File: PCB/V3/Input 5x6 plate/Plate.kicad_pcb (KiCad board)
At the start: 2 copper layers, 119.4 x 100.3 mm, 36 parts

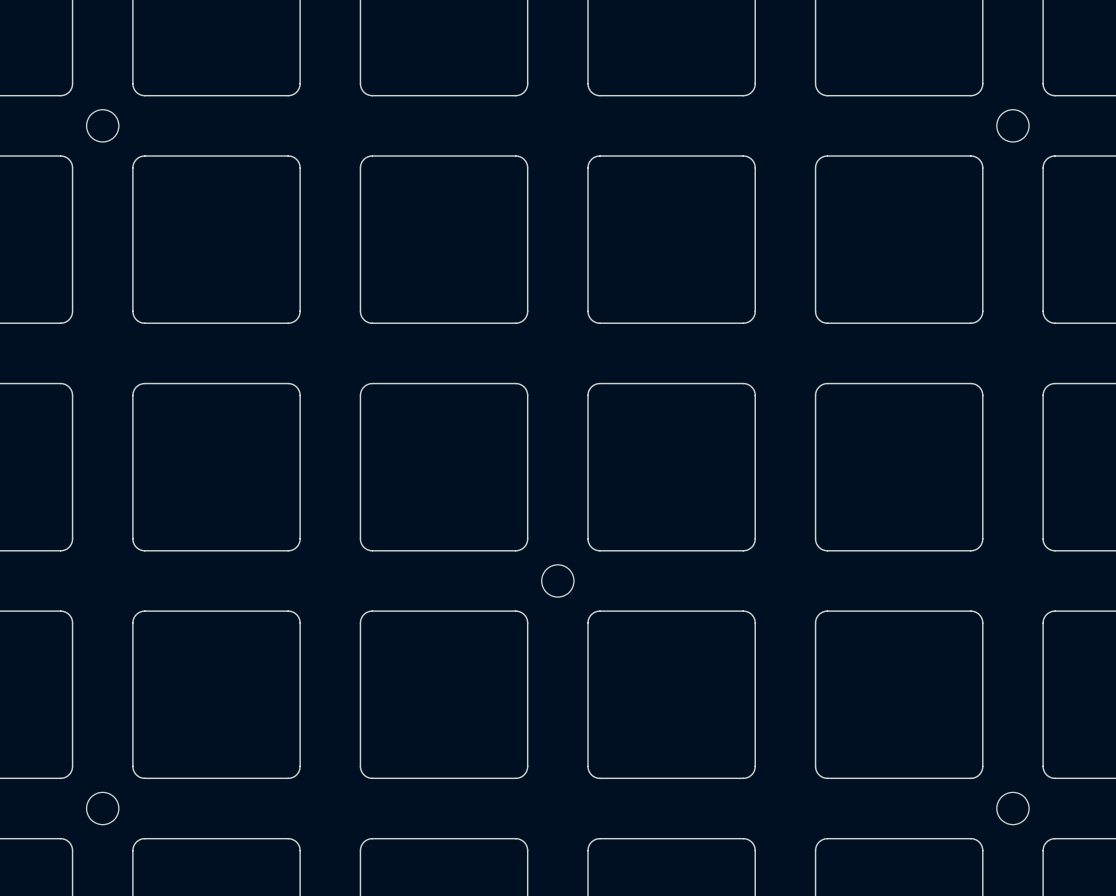
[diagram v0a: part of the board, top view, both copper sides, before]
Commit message: fix mount hole dimension
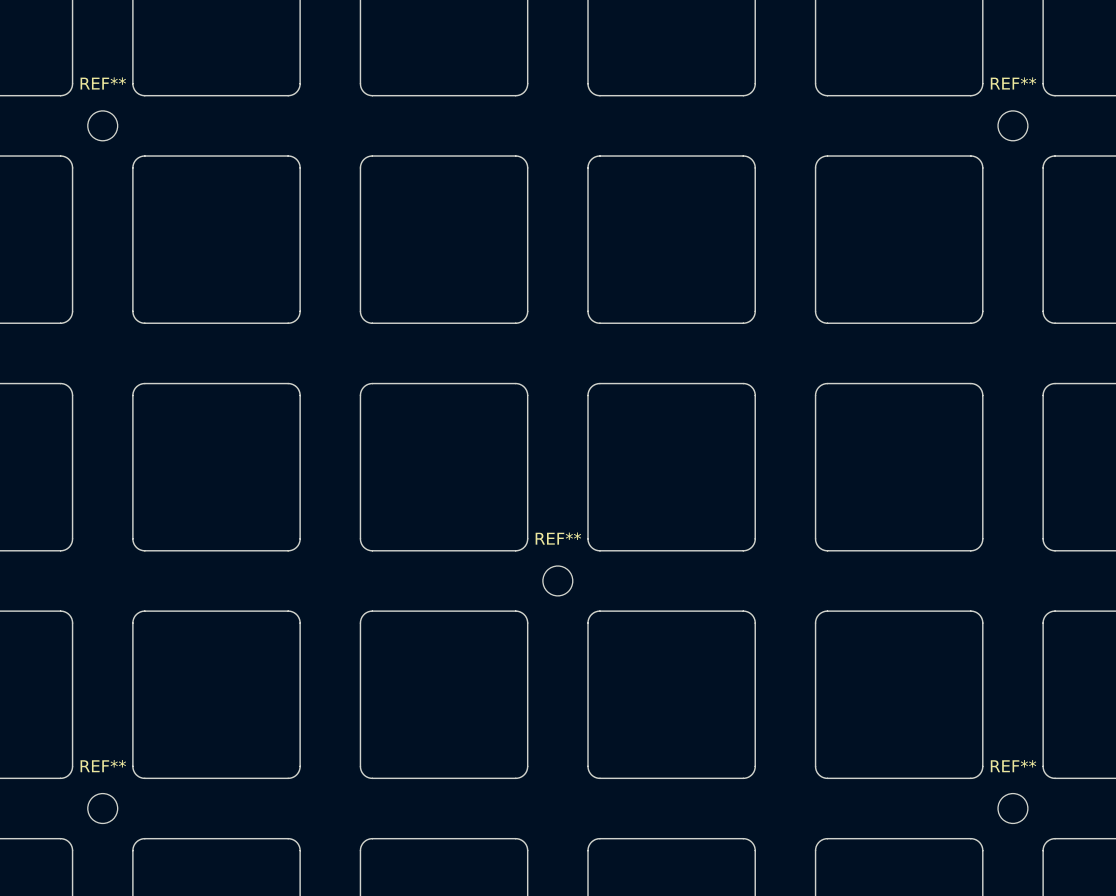
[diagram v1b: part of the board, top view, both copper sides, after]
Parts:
- REF** (x5): value MountingHole_2.7mm_M2.5 -> MountingHole_2.5mm; footprint MountingHole:MountingHole_2.7mm_M2.5 -> Keyboard_JSA:MountingHole_2.5mm
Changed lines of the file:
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@@
     (fp_arc (start 7 6) (mid 6.707107 6.707107) (end 6 7) (layer "Edge.Cuts") (width 0.12))
   )
-  (footprint "MountingHole:MountingHole_2.7mm_M2.5" (layer "F.Cu")
+  (footprint "Keyboard_JSA:MountingHole_2.5mm" (layer "F.Cu")
     (at 117.475 98.425)
-    (descr "Mounting Hole 2.7mm, no annular, M2.5")
-    (tags "mounting hole 2.7mm no annular m2.5")
+    (descr "Mounting Hole 2.5mm, no annular")
+    (tags "mounting hole 2.5mm no annular")
     (attr exclude_from_pos_files exclude_from_bom)
-    (fp_text reference "REF**" (at 0 -3.7) (layer "Dwgs.User")
-      (effects (font (size 1 1) (thickness 0.15)))
-    )
-    (fp_text value "MountingHole_2.7mm_M2.5" (at 0 3.7) (layer "F.Fab")
-      (effects (font (size 1 1) (thickness 0.15)))
-    )
-    (fp_text user "${REFERENCE}" (at 0.3 0) (layer "F.Fab")
-      (effects (font (size 1 1) (thickness 0.15)))
-    )
-    (fp_circle (center 0 0) (end 2.7 0) (layer "Cmts.User") (width 0.15) (fill none))
-    (fp_circle (center 0 0) (end 2.95 0) (layer "F.CrtYd") (width 0.05) (fill none))
-    (pad "" np_thru_hole circle (at 0 0) (size 2.7 2.7) (drill 2.7) (layers *.Cu *.Mask))
+    (fp_text reference "REF**" (at 0 -3.5) (layer "F.SilkS")
+      (effects (font (size 1 1) (thickness 0.15)))
+    )
+    (fp_text value "MountingHole_2.5mm" (at 0 3.5) (layer "F.Fab")
+      (effects (font (size 1 1) (thickness 0.15)))
+    )
+    (fp_text user "${REFERENCE}" (at 0 0) (layer "F.Fab")
+      (effects (font (size 1 1) (thickness 0.15)))
+    )
+    (fp_circle (center 0 0) (end 2.5 0) (layer "Cmts.User") (width 0.15) (fill none))
+    (fp_circle (center 0 0) (end 2.75 0) (layer "F.CrtYd") (width 0.05) (fill none))
+    (pad "" np_thru_hole circle (at 0 0) (size 2.5 2.5) (drill 2.5) (layers *.Cu *.Mask))
   )
   (footprint "Keyboard_JSA:Switch_Hole_Cutout_w_Deco" (layer "F.Cu")
@@
     (fp_arc (start 7 6) (mid 6.707107 6.707107) (end 6 7) (layer "Edge.Cuts") (width 0.12))
   )
-  (footprint "MountingHole:MountingHole_2.7mm_M2.5" (layer "F.Cu")
+  (footprint "Keyboard_JSA:MountingHole_2.5mm" (layer "F.Cu")
     (at 41.275 41.275)
-    (descr "Mounting Hole 2.7mm, no annular, M2.5")
-    (tags "mounting hole 2.7mm no annular m2.5")
+    (descr "Mounting Hole 2.5mm, no annular")
+    (tags "mounting hole 2.5mm no annular")
     (attr exclude_from_pos_files exclude_from_bom)
-    (fp_text reference "REF**" (at 0 -3.7) (layer "Dwgs.User")
-      (effects (font (size 1 1) (thickness 0.15)))
-    )
-    (fp_text value "MountingHole_2.7mm_M2.5" (at 0 3.7) (layer "F.Fab")
-      (effects (font (size 1 1) (thickness 0.15)))
-    )
-    (fp_text user "${REFERENCE}" (at 0.3 0) (layer "F.Fab")
-      (effects (font (size 1 1) (thickness 0.15)))
-    )
-    (fp_circle (center 0 0) (end 2.7 0) (layer "Cmts.User") (width 0.15) (fill none))
-    (fp_circle (center 0 0) (end 2.95 0) (layer "F.CrtYd") (width 0.05) (fill none))
-    (pad "" np_thru_hole circle (at 0 0) (size 2.7 2.7) (drill 2.7) (layers *.Cu *.Mask))
+    (fp_text reference "REF**" (at 0 -3.5) (layer "F.SilkS")
+      (effects (font (size 1 1) (thickness 0.15)))
+    )
+    (fp_text value "MountingHole_2.5mm" (at 0 3.5) (layer "F.Fab")
+      (effects (font (size 1 1) (thickness 0.15)))
+    )
+    (fp_text user "${REFERENCE}" (at 0 0) (layer "F.Fab")
+      (effects (font (size 1 1) (thickness 0.15)))
+    )
+    (fp_circle (center 0 0) (end 2.5 0) (layer "Cmts.User") (width 0.15) (fill none))
+    (fp_circle (center 0 0) (end 2.75 0) (layer "F.CrtYd") (width 0.05) (fill none))
+    (pad "" np_thru_hole circle (at 0 0) (size 2.5 2.5) (drill 2.5) (layers *.Cu *.Mask))
   )
   (footprint "Keyboard_JSA:Switch_Hole_Cutout_w_Deco" (layer "F.Cu")
@@
     (fp_arc (start -6 7) (mid -6.707107 6.707107) (end -7 6) (layer "Edge.Cuts") (width 0.12))
   )
-  (footprint "MountingHole:MountingHole_2.7mm_M2.5" (layer "F.Cu")
+  (footprint "Keyboard_JSA:MountingHole_2.5mm" (layer "F.Cu")
     (at 79.375 79.375)
-    (descr "Mounting Hole 2.7mm, no annular, M2.5")
-    (tags "mounting hole 2.7mm no annular m2.5")
+    (descr "Mounting Hole 2.5mm, no annular")
+    (tags "mounting hole 2.5mm no annular")
     (attr exclude_from_pos_files exclude_from_bom)
-    (fp_text reference "REF**" (at 0 -3.7) (layer "Dwgs.User")
-      (effects (font (size 1 1) (thickness 0.15)))
-    )
-    (fp_text value "MountingHole_2.7mm_M2.5" (at 0 3.7) (layer "F.Fab")
-      (effects (font (size 1 1) (thickness 0.15)))
-    )
-    (fp_text user "${REFERENCE}" (at 0.3 0) (layer "F.Fab")
-      (effects (font (size 1 1) (thickness 0.15)))
-    )
-    (fp_circle (center 0 0) (end 2.7 0) (layer "Cmts.User") (width 0.15) (fill none))
-    (fp_circle (center 0 0) (end 2.95 0) (layer "F.CrtYd") (width 0.05) (fill none))
-    (pad "" np_thru_hole circle (at 0 0) (size 2.7 2.7) (drill 2.7) (layers *.Cu *.Mask))
+    (fp_text reference "REF**" (at 0 -3.5) (layer "F.SilkS")
+      (effects (font (size 1 1) (thickness 0.15)))
+    )
+    (fp_text value "MountingHole_2.5mm" (at 0 3.5) (layer "F.Fab")
+      (effects (font (size 1 1) (thickness 0.15)))
+    )
+    (fp_text user "${REFERENCE}" (at 0 0) (layer "F.Fab")
+      (effects (font (size 1 1) (thickness 0.15)))
+    )
+    (fp_circle (center 0 0) (end 2.5 0) (layer "Cmts.User") (width 0.15) (fill none))
+    (fp_circle (center 0 0) (end 2.75 0) (layer "F.CrtYd") (width 0.05) (fill none))
+    (pad "" np_thru_hole circle (at 0 0) (size 2.5 2.5) (drill 2.5) (layers *.Cu *.Mask))
   )
   (footprint "Keyboard_JSA:Switch_Hole_Cutout_w_Deco" (layer "F.Cu")
@@
     (fp_arc (start -7 -6) (mid -6.707107 -6.707107) (end -6 -7) (layer "Edge.Cuts") (width 0.12))
   )
-  (footprint "MountingHole:MountingHole_2.7mm_M2.5" (layer "F.Cu")
+  (footprint "Keyboard_JSA:MountingHole_2.5mm" (layer "F.Cu")
     (at 117.475 41.275)
-    (descr "Mounting Hole 2.7mm, no annular, M2.5")
-    (tags "mounting hole 2.7mm no annular m2.5")
+    (descr "Mounting Hole 2.5mm, no annular")
+    (tags "mounting hole 2.5mm no annular")
     (attr exclude_from_pos_files exclude_from_bom)
-    (fp_text reference "REF**" (at 0 -3.7) (layer "Dwgs.User")
-      (effects (font (size 1 1) (thickness 0.15)))
-    )
-    (fp_text value "MountingHole_2.7mm_M2.5" (at 0 3.7) (layer "F.Fab")
-      (effects (font (size 1 1) (thickness 0.15)))
-    )
-    (fp_text user "${REFERENCE}" (at 0.3 0) (layer "F.Fab")
-      (effects (font (size 1 1) (thickness 0.15)))
-    )
-    (fp_circle (center 0 0) (end 2.7 0) (layer "Cmts.User") (width 0.15) (fill none))
-    (fp_circle (center 0 0) (end 2.95 0) (layer "F.CrtYd") (width 0.05) (fill none))
-    (pad "" np_thru_hole circle (at 0 0) (size 2.7 2.7) (drill 2.7) (layers *.Cu *.Mask))
-  )
-  (footprint "MountingHole:MountingHole_2.7mm_M2.5" (layer "F.Cu")
+    (fp_text reference "REF**" (at 0 -3.5) (layer "F.SilkS")
+      (effects (font (size 1 1) (thickness 0.15)))
+    )
+    (fp_text value "MountingHole_2.5mm" (at 0 3.5) (layer "F.Fab")
+      (effects (font (size 1 1) (thickness 0.15)))
+    )
+    (fp_text user "${REFERENCE}" (at 0 0) (layer "F.Fab")
+      (effects (font (size 1 1) (thickness 0.15)))
+    )
+    (fp_circle (center 0 0) (end 2.5 0) (layer "Cmts.User") (width 0.15) (fill none))
+    (fp_circle (center 0 0) (end 2.75 0) (layer "F.CrtYd") (width 0.05) (fill none))
+    (pad "" np_thru_hole circle (at 0 0) (size 2.5 2.5) (drill 2.5) (layers *.Cu *.Mask))
+  )
+  (footprint "Keyboard_JSA:MountingHole_2.5mm" (layer "F.Cu")
     (at 41.275 98.425)
-    (descr "Mounting Hole 2.7mm, no annular, M2.5")
-    (tags "mounting hole 2.7mm no annular m2.5")
+    (descr "Mounting Hole 2.5mm, no annular")
+    (tags "mounting hole 2.5mm no annular")
     (attr exclude_from_pos_files exclude_from_bom)
-    (fp_text reference "REF**" (at 0 -3.7) (layer "Dwgs.User")
-      (effects (font (size 1 1) (thickness 0.15)))
-    )
-    (fp_text value "MountingHole_2.7mm_M2.5" (at 0 3.7) (layer "F.Fab")
-      (effects (font (size 1 1) (thickness 0.15)))
-    )
-    (fp_text user "${REFERENCE}" (at 0.3 0) (layer "F.Fab")
-      (effects (font (size 1 1) (thickness 0.15)))
-    )
-    (fp_circle (center 0 0) (end 2.7 0) (layer "Cmts.User") (width 0.15) (fill none))
-    (fp_circle (center 0 0) (end 2.95 0) (layer "F.CrtYd") (width 0.05) (fill none))
-    (pad "" np_thru_hole circle (at 0 0) (size 2.7 2.7) (drill 2.7) (layers *.Cu *.Mask))
-  )
-  (footprint "Keyboard_JSA:Switch_Hole_Cutout_w_Deco" (layer "F.Cu")
+    (fp_text reference "REF**" (at 0 -3.5) (layer "F.SilkS")
+      (effects (font (size 1 1) (thickness 0.15)))
+    )
+    (fp_text value "MountingHole_2.5mm" (at 0 3.5) (layer "F.Fab")
+      (effects (font (size 1 1) (thickness 0.15)))
+    )
+    (fp_text user "${REFERENCE}" (at 0 0) (layer "F.Fab")
+      (effects (font (size 1 1) (thickness 0.15)))
+    )
+    (fp_circle (center 0 0) (end 2.5 0) (layer "Cmts.User") (width 0.15) (fill none))
+    (fp_circle (center 0 0) (end 2.75 0) (layer "F.CrtYd") (width 0.05) (fill none))
+    (pad "" np_thru_hole circle (at 0 0) (size 2.5 2.5) (drill 2.5) (layers *.Cu *.Mask))
+  )
+  (footprint "Keyboard_JSA:Switch_Hole_Cutout_w_Deco" (layer "F.Cu")
